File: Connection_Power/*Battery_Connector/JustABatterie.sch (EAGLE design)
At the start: 2 parts

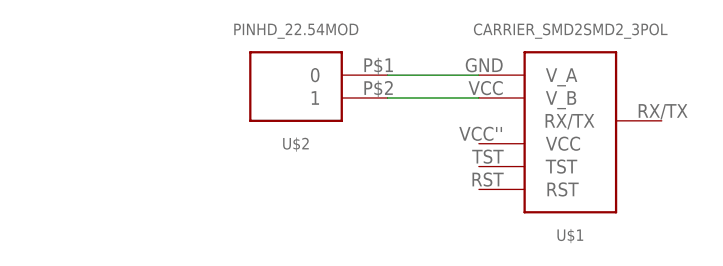
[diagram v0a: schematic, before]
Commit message: Update Pinheader
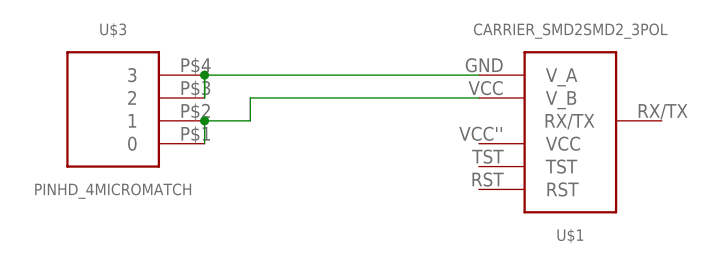
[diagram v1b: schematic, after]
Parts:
- removed U$2: PINHD_22.54MOD, thar:PINHD_22.54MOD
- added U$3: PINHD_4MICROMATCH, thar:PINHD_4MICROMATCH
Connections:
- net N$2: now also U$3.2, U$3.3; no longer U$2.0
- net N$3: now also U$3.0, U$3.1; no longer U$2.1
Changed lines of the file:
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@@
 <grid distance="0.1" unitdist="inch" unit="inch" style="lines" multiple="1" display="no" altdistance="0.01" altunitdist="inch" altunit="inch"/>
 <layers>
-<layer number="1" name="Top" color="4" fill="1" visible="yes" active="no"/>
-<layer number="16" name="Bottom" color="1" fill="1" visible="yes" active="no"/>
-<layer number="17" name="Pads" color="2" fill="1" visible="yes" active="no"/>
-<layer number="18" name="Vias" color="2" fill="1" visible="yes" active="no"/>
-<layer number="19" name="Unrouted" color="6" fill="1" visible="yes" active="no"/>
-<layer number="20" name="Dimension" color="15" fill="1" visible="yes" active="no"/>
-<layer number="21" name="tPlace" color="7" fill="1" visible="yes" active="no"/>
-<layer number="22" name="bPlace" color="7" fill="1" visible="yes" active="no"/>
-<layer number="23" name="tOrigins" color="15" fill="1" visible="yes" active="no"/>
-<layer number="24" name="bOrigins" color="15" fill="1" visible="yes" active="no"/>
-<layer number="25" name="tNames" color="7" fill="1" visible="yes" active="no"/>
-<layer number="26" name="bNames" color="7" fill="1" visible="yes" active="no"/>
-<layer number="27" name="tValues" color="7" fill="1" visible="yes" active="no"/>
-<layer number="28" name="bValues" color="7" fill="1" visible="yes" active="no"/>
+<layer number="1" name="Top" color="4" fill="1" visible="no" active="no"/>
+<layer number="16" name="Bottom" color="1" fill="1" visible="no" active="no"/>
+<layer number="17" name="Pads" color="2" fill="1" visible="no" active="no"/>
+<layer number="18" name="Vias" color="2" fill="1" visible="no" active="no"/>
+<layer number="19" name="Unrouted" color="6" fill="1" visible="no" active="no"/>
+<layer number="20" name="Dimension" color="15" fill="1" visible="no" active="no"/>
+<layer number="21" name="tPlace" color="7" fill="1" visible="no" active="no"/>
+<layer number="22" name="bPlace" color="7" fill="1" visible="no" active="no"/>
+<layer number="23" name="tOrigins" color="15" fill="1" visible="no" active="no"/>
+<layer number="24" name="bOrigins" color="15" fill="1" visible="no" active="no"/>
+<layer number="25" name="tNames" color="7" fill="1" visible="no" active="no"/>
+<layer number="26" name="bNames" color="7" fill="1" visible="no" active="no"/>
+<layer number="27" name="tValues" color="7" fill="1" visible="no" active="no"/>
+<layer number="28" name="bValues" color="7" fill="1" visible="no" active="no"/>
 <layer number="29" name="tStop" color="7" fill="3" visible="no" active="no"/>
 <layer number="30" name="bStop" color="7" fill="6" visible="no" active="no"/>
@@
 <layer number="35" name="tGlue" color="7" fill="4" visible="no" active="no"/>
 <layer number="36" name="bGlue" color="7" fill="5" visible="no" active="no"/>
-<layer number="37" name="tTest" color="7" fill="1" visible="yes" active="no"/>
-<layer number="38" name="bTest" color="7" fill="1" visible="yes" active="no"/>
+<layer number="37" name="tTest" color="7" fill="1" visible="no" active="no"/>
+<layer number="38" name="bTest" color="7" fill="1" visible="no" active="no"/>
 <layer number="39" name="tKeepout" color="4" fill="11" visible="no" active="no"/>
 <layer number="40" name="bKeepout" color="1" fill="11" visible="no" active="no"/>
@@
 <layer number="44" name="Drills" color="7" fill="1" visible="no" active="no"/>
 <layer number="45" name="Holes" color="7" fill="1" visible="no" active="no"/>
-<layer number="46" name="Milling" color="3" fill="1" visible="yes" active="no"/>
-<layer number="47" name="Measures" color="7" fill="1" visible="yes" active="no"/>
-<layer number="48" name="Document" color="7" fill="1" visible="yes" active="no"/>
-<layer number="49" name="Reference" color="7" fill="1" visible="yes" active="no"/>
-<layer number="50" name="dxf" color="7" fill="1" visible="yes" active="no"/>
-<layer number="51" name="tDocu" color="7" fill="1" visible="yes" active="no"/>
-<layer number="52" name="bDocu" color="7" fill="1" visible="yes" active="no"/>
-<layer number="53" name="tGND_GNDA" color="7" fill="9" visible="yes" active="no"/>
-<layer number="54" name="bGND_GNDA" color="1" fill="9" visible="yes" active="no"/>
-<layer number="56" name="wert" color="7" fill="1" visible="yes" active="no"/>
-<layer number="57" name="tCAD" color="7" fill="1" visible="yes" active="no"/>
+<layer number="46" name="Milling" color="3" fill="1" visible="no" active="no"/>
+<layer number="47" name="Measures" color="7" fill="1" visible="no" active="no"/>
+<layer number="48" name="Document" color="7" fill="1" visible="no" active="no"/>
+<layer number="49" name="Reference" color="7" fill="1" visible="no" active="no"/>
+<layer number="50" name="dxf" color="7" fill="1" visible="no" active="no"/>
+<layer number="51" name="tDocu" color="7" fill="1" visible="no" active="no"/>
+<layer number="52" name="bDocu" color="7" fill="1" visible="no" active="no"/>
+<layer number="53" name="tGND_GNDA" color="7" fill="9" visible="no" active="no"/>
+<layer number="54" name="bGND_GNDA" color="1" fill="9" visible="no" active="no"/>
+<layer number="56" name="wert" color="7" fill="1" visible="no" active="no"/>
+<layer number="57" name="tCAD" color="7" fill="1" visible="no" active="no"/>
+<layer number="90" name="Modules" color="5" fill="1" visible="no" active="no"/>
 <layer number="91" name="Nets" color="2" fill="1" visible="yes" active="yes"/>
 <layer number="92" name="Busses" color="1" fill="1" visible="yes" active="yes"/>
@@
 <layer number="97" name="Info" color="7" fill="1" visible="yes" active="yes"/>
 <layer number="98" name="Guide" color="6" fill="1" visible="yes" active="yes"/>
+<layer number="99" name="SpiceOrder" color="7" fill="1" visible="no" active="no"/>
 <layer number="100" name="Muster" color="7" fill="1" visible="no" active="no"/>
 <layer number="101" name="Patch_Top" color="12" fill="4" visible="yes" active="yes"/>
@@
 <layer number="111" name="LPC17xx" color="7" fill="1" visible="no" active="yes"/>
 <layer number="112" name="tSilk" color="7" fill="1" visible="no" active="yes"/>
+<layer number="113" name="IDFDebug" color="7" fill="1" visible="yes" active="yes"/>
 <layer number="116" name="Patch_BOT" color="9" fill="4" visible="yes" active="yes"/>
 <layer number="118" name="Rect_Pads" color="7" fill="1" visible="no" active="yes"/>
@@
 <part name="FRAME1" library="frames" deviceset="A5L-LOC" device=""/>
 <part name="U$1" library="thar" deviceset="CARRIER_SMD2" device="SMD2_3POL" value="CARRIER_SMD2SMD2_3POL"/>
-<part name="U$2" library="thar" deviceset="PINHD_2" device="2.54MOD"/>
+<part name="U$3" library="thar" deviceset="PINHD_4" device="MICROMATCH"/>
 </parts>
 <sheets>
@@
 <instance part="FRAME1" gate="G$1" x="0" y="0"/>
 <instance part="U$1" gate="A" x="167.64" y="96.52"/>
-<instance part="U$2" gate="G$1" x="137.16" y="104.14" rot="MR0"/>
+<instance part="U$3" gate="G$1" x="116.84" y="101.6" rot="R180"/>
 </instances>
 <busses>
@@
 <segment>
 <pinref part="U$1" gate="A" pin="V_A"/>
-<pinref part="U$2" gate="G$1" pin="0"/>
-<wire x1="147.32" y1="106.68" x2="157.48" y2="106.68" width="0.1524" layer="91"/>
+<wire x1="157.48" y1="106.68" x2="127" y2="106.68" width="0.1524" layer="91"/>
+<wire x1="127" y1="106.68" x2="127" y2="104.14" width="0.1524" layer="91"/>
+<pinref part="U$3" gate="G$1" pin="3"/>
+<pinref part="U$3" gate="G$1" pin="2"/>
+<wire x1="127" y1="106.68" x2="127" y2="104.14" width="0.1524" layer="91"/>
+<junction x="127" y="106.68"/>
 </segment>
 </net>
@@
 <segment>
 <pinref part="U$1" gate="A" pin="V_B"/>
-<pinref part="U$2" gate="G$1" pin="1"/>
-<wire x1="147.32" y1="104.14" x2="157.48" y2="104.14" width="0.1524" layer="91"/>
+<wire x1="157.48" y1="104.14" x2="132.08" y2="104.14" width="0.1524" layer="91"/>
+<wire x1="132.08" y1="104.14" x2="132.08" y2="101.6" width="0.1524" layer="91"/>
+<pinref part="U$3" gate="G$1" pin="1"/>
+<pinref part="U$3" gate="G$1" pin="0"/>
+<wire x1="127" y1="101.6" x2="127" y2="99.06" width="0.1524" layer="91"/>
+<wire x1="132.08" y1="101.6" x2="127" y2="101.6" width="0.1524" layer="91"/>
+<junction x="127" y="101.6"/>
 </segment>
 </net>
